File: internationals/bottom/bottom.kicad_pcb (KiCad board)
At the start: 2 copper layers, 1 part, among them U1 ESP-S2-Pico

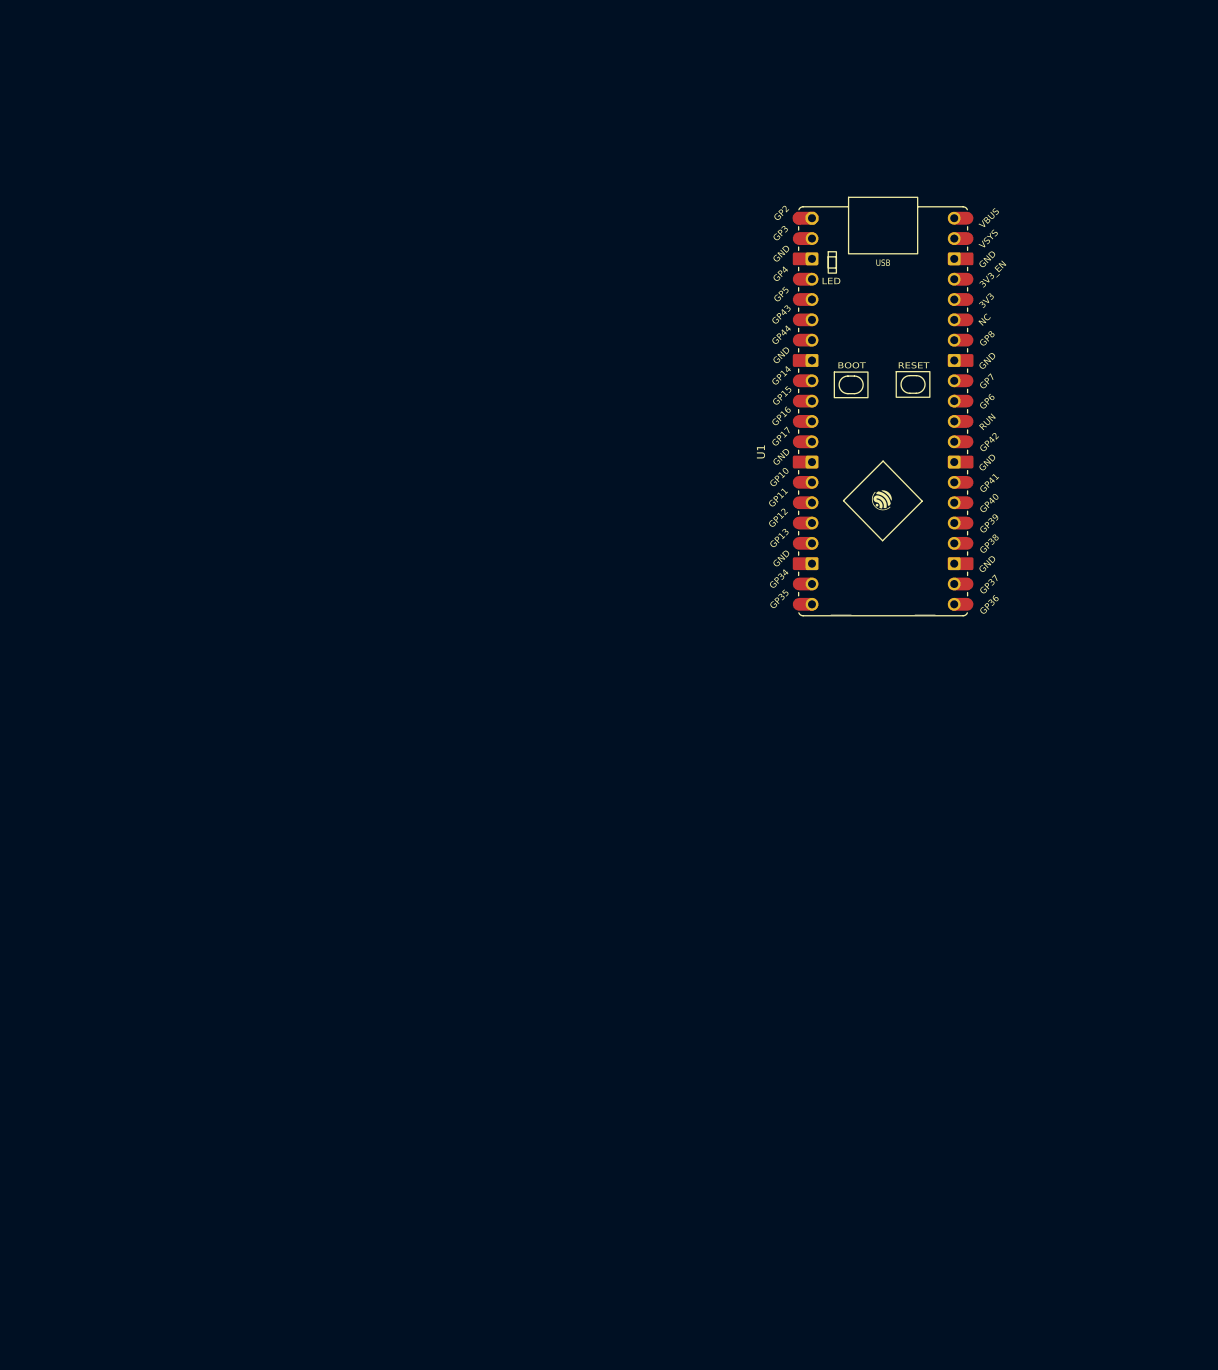
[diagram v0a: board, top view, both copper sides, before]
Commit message: pcbs: bottom: feat: add pcb with parts placed, left with routing
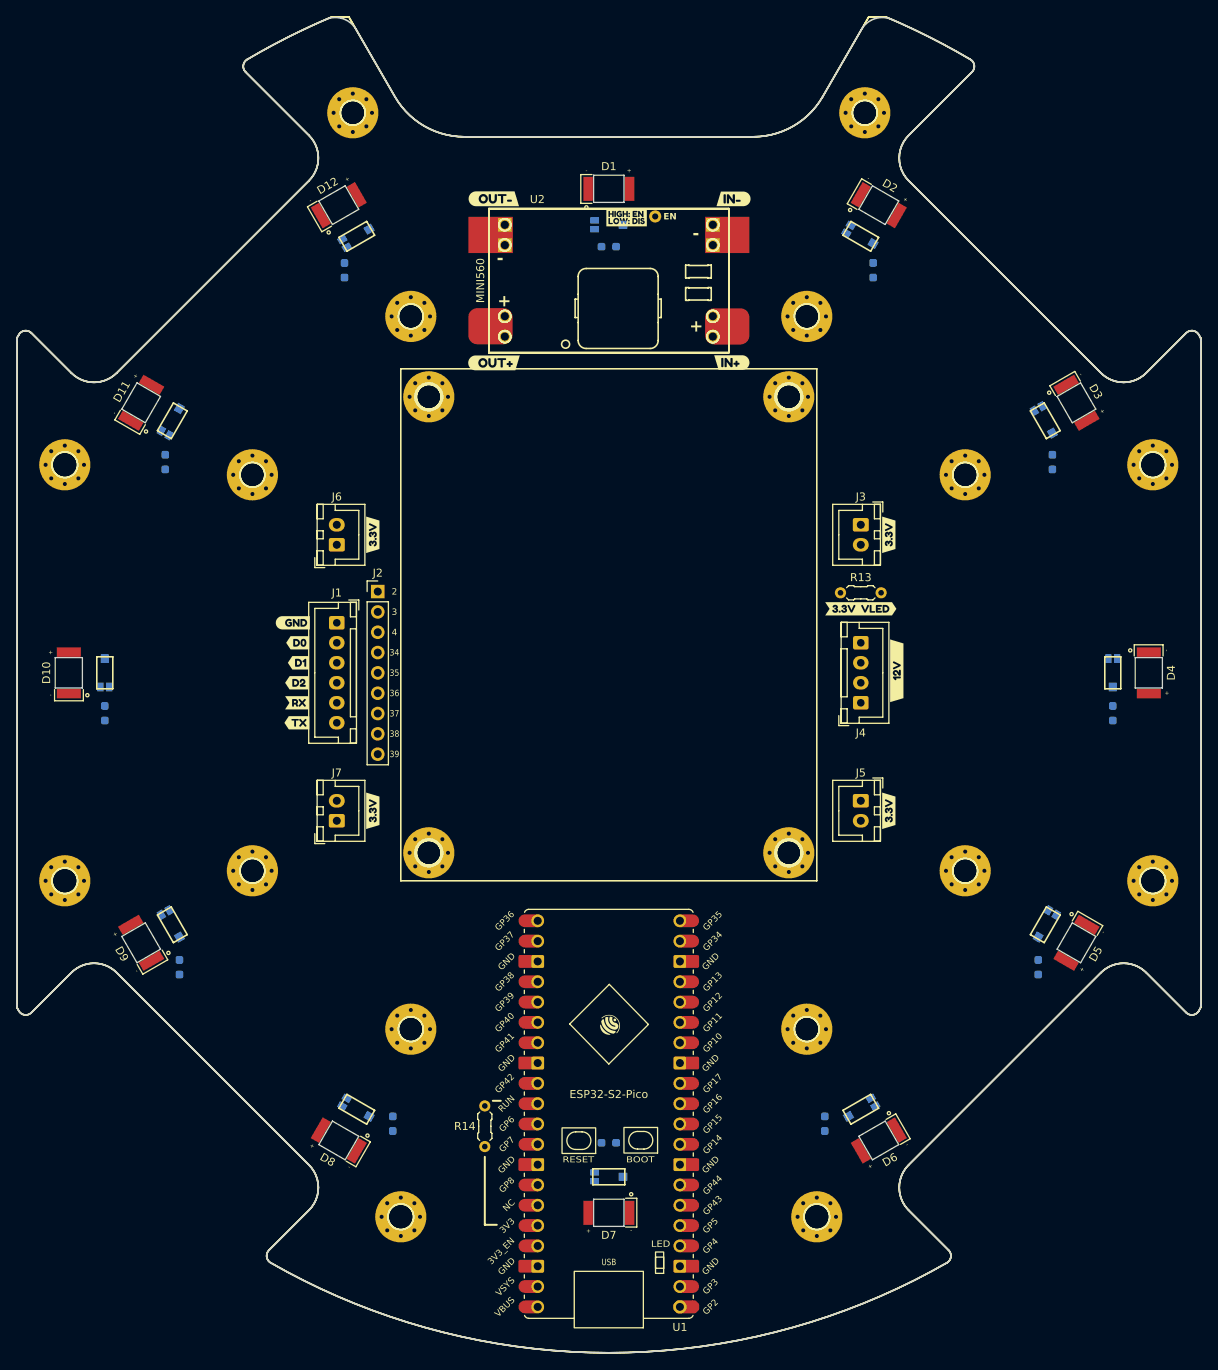
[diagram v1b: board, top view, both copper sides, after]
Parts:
- added D1: LED, PorridgePi-Personal:LED-6028-SMD, F.Cu at (100.0, 39.5)
- added D10: LED, PorridgePi-Personal:LED-6028-SMD, F.Cu at (32.5, 100.0)
- added D11: LED, PorridgePi-Personal:LED-6028-SMD, F.Cu at (41.5, 66.2)
- added D12: LED, PorridgePi-Personal:LED-6028-SMD, F.Cu at (66.2, 41.5)
- added D2: LED, PorridgePi-Personal:LED-6028-SMD, F.Cu at (133.8, 41.5)
- added D3: LED, PorridgePi-Personal:LED-6028-SMD, F.Cu at (158.5, 66.2)
- added D4: LED, PorridgePi-Personal:LED-6028-SMD, F.Cu at (167.5, 100.0)
- added D5: LED, PorridgePi-Personal:LED-6028-SMD, F.Cu at (158.5, 133.8)
- added D6: LED, PorridgePi-Personal:LED-6028-SMD, F.Cu at (133.8, 158.5)
- added D7: LED, PorridgePi-Personal:LED-6028-SMD, F.Cu at (100.0, 167.5)
- added D8: LED, PorridgePi-Personal:LED-6028-SMD, F.Cu at (66.2, 158.5)
- added D9: LED, PorridgePi-Personal:LED-6028-SMD, F.Cu at (41.5, 133.8)
- added H1: MountingHole-M3, MountingHole:MountingHole_3.2mm_M3_Pad_Via, F.Cu at (68.0, 30.0)
- added H10: MountingHole-M3, MountingHole:MountingHole_3.2mm_M3_Pad_Via, F.Cu at (55.5, 75.3)
- added H11: MountingHole-M3, MountingHole:MountingHole_3.2mm_M3_Pad_Via, F.Cu at (55.5, 124.7)
- added H12: MountingHole-M3, MountingHole:MountingHole_3.2mm_M3_Pad_Via, F.Cu at (75.3, 144.5)
- added H13: MountingHole-M3, MountingHole:MountingHole_3.2mm_M3_Pad_Via, F.Cu at (144.5, 75.3)
- added H14: MountingHole-M3, MountingHole:MountingHole_3.2mm_M3_Pad_Via, F.Cu at (144.5, 124.7)
- added H15: MountingHole-M3, MountingHole:MountingHole_3.2mm_M3_Pad_Via, F.Cu at (124.7, 144.5)
- added H16: MountingHole-M3, MountingHole:MountingHole_3.2mm_M3_Pad_Via, F.Cu at (124.7, 55.5)
- added H17: MountingHole-M3, MountingHole:MountingHole_3.2mm_M3_Pad_Via, F.Cu at (122.5, 122.5)
- added H18: MountingHole-M3, MountingHole:MountingHole_3.2mm_M3_Pad_Via, F.Cu at (77.5, 122.5)
- added H19: MountingHole-M3, MountingHole:MountingHole_3.2mm_M3_Pad_Via, F.Cu at (77.5, 65.5)
- added H2: MountingHole-M3, MountingHole:MountingHole_3.2mm_M3_Pad_Via, F.Cu at (132.0, 30.0)
- added H20: MountingHole-M3, MountingHole:MountingHole_3.2mm_M3_Pad_Via, F.Cu at (122.5, 65.5)
- added H3: MountingHole-M3, MountingHole:MountingHole_3.2mm_M3_Pad_Via, F.Cu at (168.0, 74.0)
- added H4: MountingHole-M3, MountingHole:MountingHole_3.2mm_M3_Pad_Via, F.Cu at (168.0, 126.0)
- added H5: MountingHole-M3, MountingHole:MountingHole_3.2mm_M3_Pad_Via, F.Cu at (126.0, 168.0)
- added H6: MountingHole-M3, MountingHole:MountingHole_3.2mm_M3_Pad_Via, F.Cu at (74.0, 168.0)
- added H7: MountingHole-M3, MountingHole:MountingHole_3.2mm_M3_Pad_Via, F.Cu at (32.0, 74.0)
- added H8: MountingHole-M3, MountingHole:MountingHole_3.2mm_M3_Pad_Via, F.Cu at (32.0, 126.0)
- added H9: MountingHole-M3, MountingHole:MountingHole_3.2mm_M3_Pad_Via, F.Cu at (75.3, 55.5)
- added J1: JST-XH-B6B, Connector_JST:JST_XH_B6B-XH-A_1x06_P2.50mm_Vertical, F.Cu at (66.0, 93.8)
- added J2: Header-01x09, Connector_PinHeader_2.54mm:PinHeader_1x09_P2.54mm_Vertical, F.Cu at (71.1, 89.8)
- added J3: 3.3V-JST-XH-B2B, Connector_JST:JST_XH_B2B-XH-A_1x02_P2.50mm_Vertical, F.Cu at (131.5, 81.5)
- added J4: JST-XH-B4B, Connector_JST:JST_XH_B4B-XH-A_1x04_P2.50mm_Vertical, F.Cu at (131.5, 103.8)
- added J5: 3.3V-JST-XH-B2B, Connector_JST:JST_XH_B2B-XH-A_1x02_P2.50mm_Vertical, F.Cu at (131.5, 116.0)
- added J6: 3.3V-JST-XH-B2B, Connector_JST:JST_XH_B2B-XH-A_1x02_P2.50mm_Vertical, F.Cu at (66.0, 84.0)
- added J7: 3.3V-JST-XH-B2B, Connector_JST:JST_XH_B2B-XH-A_1x02_P2.50mm_Vertical, F.Cu at (66.0, 118.5)
- added L1: TEMT6000, PorridgePi-Personal:TEMT6000-SMD, B.Cu at (100.0, 44.0)
- added L10: TEMT6000, PorridgePi-Personal:TEMT6000-SMD, B.Cu at (37.0, 100.0)
- added L11: TEMT6000, PorridgePi-Personal:TEMT6000-SMD, B.Cu at (45.4, 68.5)
- added L12: TEMT6000, PorridgePi-Personal:TEMT6000-SMD, B.Cu at (68.5, 45.4)
- added L2: TEMT6000, PorridgePi-Personal:TEMT6000-SMD, B.Cu at (131.5, 45.4)
- added L3: TEMT6000, PorridgePi-Personal:TEMT6000-SMD, B.Cu at (154.6, 68.5)
- added L4: TEMT6000, PorridgePi-Personal:TEMT6000-SMD, B.Cu at (163.0, 100.0)
- added L5: TEMT6000, PorridgePi-Personal:TEMT6000-SMD, B.Cu at (154.6, 131.5)
- added L6: TEMT6000, PorridgePi-Personal:TEMT6000-SMD, B.Cu at (131.5, 154.6)
- added L7: TEMT6000, PorridgePi-Personal:TEMT6000-SMD, B.Cu at (100.0, 163.0)
- added L8: TEMT6000, PorridgePi-Personal:TEMT6000-SMD, B.Cu at (68.5, 154.6)
- added L9: TEMT6000, PorridgePi-Personal:TEMT6000-SMD, B.Cu at (45.4, 131.5)
- added R1: 10k, Resistor_SMD:R_0603_1608Metric_Pad0.98x0.95mm_HandSolder, B.Cu at (100.0, 46.7)
- added R10: 10k, Resistor_SMD:R_0603_1608Metric_Pad0.98x0.95mm_HandSolder, B.Cu at (37.0, 105.1)
- added R11: 10k, Resistor_SMD:R_0603_1608Metric_Pad0.98x0.95mm_HandSolder, B.Cu at (44.6, 73.7)
- added R12: 10k, Resistor_SMD:R_0603_1608Metric_Pad0.98x0.95mm_HandSolder, B.Cu at (67.0, 49.7)
- added R13: R, PCM_Resistor_THT_AKL:R_Axial_DIN0204_L3.6mm_D1.6mm_P5.08mm_Horizontal, F.Cu at (129.0, 90.0)
- added R14: R, PCM_Resistor_THT_AKL:R_Axial_DIN0204_L3.6mm_D1.6mm_P5.08mm_Horizontal, F.Cu at (84.5, 154.1)
- added R2: 10k, Resistor_SMD:R_0603_1608Metric_Pad0.98x0.95mm_HandSolder, B.Cu at (133.0, 49.7)
- added R3: 10k, Resistor_SMD:R_0603_1608Metric_Pad0.98x0.95mm_HandSolder, B.Cu at (155.4, 73.7)
- added R4: 10k, Resistor_SMD:R_0603_1608Metric_Pad0.98x0.95mm_HandSolder, B.Cu at (163.0, 105.1)
- added R5: 10k, Resistor_SMD:R_0603_1608Metric_Pad0.98x0.95mm_HandSolder, B.Cu at (153.7, 136.8)
- added R6: 10k, Resistor_SMD:R_0603_1608Metric_Pad0.98x0.95mm_HandSolder, B.Cu at (127.0, 156.4)
- added R7: 10k, Resistor_SMD:R_0603_1608Metric_Pad0.98x0.95mm_HandSolder, B.Cu at (100.0, 158.8)
- added R8: 10k, Resistor_SMD:R_0603_1608Metric_Pad0.98x0.95mm_HandSolder, B.Cu at (73.0, 156.4)
- added R9: 10k, Resistor_SMD:R_0603_1608Metric_Pad0.98x0.95mm_HandSolder, B.Cu at (46.3, 136.8)
- added U2: MINI560 3.3V, PorridgePi-Personal:MINI560, F.Cu at (87.0, 44.0)
- added kibuzzard-6669C5DE: G***, kibuzzard-6669C5DE, F.Cu at (131.5, 92.0)
- added kibuzzard-6669C5ED: G***, kibuzzard-6669C5ED, F.Cu at (70.5, 82.8)
- added kibuzzard-6669C5ED: G***, kibuzzard-6669C5ED, F.Cu at (135.0, 82.8)
- added kibuzzard-6669C5ED: G***, kibuzzard-6669C5ED, F.Cu at (135.0, 117.2)
- added kibuzzard-6669C5ED: G***, kibuzzard-6669C5ED, F.Cu at (70.5, 117.2)
- added kibuzzard-6669C688: G***, kibuzzard-6669C688, F.Cu at (136.0, 99.8)
- added kibuzzard-6669C6B5: G***, kibuzzard-6669C6B5, F.Cu at (61.2, 98.8)
- added kibuzzard-6669C6DE: G***, kibuzzard-6669C6DE, F.Cu at (61.0, 103.8)
- added kibuzzard-6669C6E8: G***, kibuzzard-6669C6E8, F.Cu at (61.0, 106.2)
- added kibuzzard-6669C6EF: G***, kibuzzard-6669C6EF, F.Cu at (60.5, 93.8)
- added kibuzzard-6669C702: G***, kibuzzard-6669C702, F.Cu at (61.1, 96.2)
- added kibuzzard-6669C706: G***, kibuzzard-6669C706, F.Cu at (61.0, 101.2)
- added kibuzzard-6669C956: G***, kibuzzard-6669C956, B.Cu at (129.2, 117.2)
- added kibuzzard-6669C956: G***, kibuzzard-6669C956, B.Cu at (63.5, 82.8)
- added kibuzzard-6669C956: G***, kibuzzard-6669C956, B.Cu at (63.5, 117.2)
- added kibuzzard-6669C956: G***, kibuzzard-6669C956, B.Cu at (129.2, 82.8)
- added kibuzzard-6669C9E8: G***, kibuzzard-6669C9E8, B.Cu at (128.5, 100.0)
- moved U1 137.1 mm to (108.9, 179.3), turned to 180 degrees
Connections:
- U1 pad 1: unconnected-(U1-GPIO2-ADC1_1-Pad1) -> GPIO2
- U1 pad 10: unconnected-(U1-GPIO15-ADC2_4-Pad10) -> TEMT3
- U1 pad 11: unconnected-(U1-GPIO16-ADC2_5-Pad11) -> TEMT4
- U1 pad 12: unconnected-(U1-GPIO17-ADC2_6-Pad12) -> TEMT5
- U1 pad 13: unconnected-(U1-GND-Pad13) -> GND
- U1 pad 14: unconnected-(U1-GPIO10-ADC1_9-Pad14) -> TEMT6
- U1 pad 15: unconnected-(U1-GPIO11-ADC2_0-Pad15) -> TEMT7
- U1 pad 16: unconnected-(U1-GPIO12-ADC2_1-Pad16) -> TEMT8
- U1 pad 17: unconnected-(U1-GPIO13-ADC2_2-Pad17) -> TEMT9
- U1 pad 18: unconnected-(U1-GND-Pad18) -> GND
- U1 pad 19: unconnected-(U1-GPIO34-Pad19) -> GPIO34
- U1 pad 2: unconnected-(U1-GPIO3-ADC1_2-Pad2) -> GPIO3
- U1 pad 20: unconnected-(U1-GPIO35-Pad20) -> GPIO35
- U1 pad 21: unconnected-(U1-GPIO36-Pad21) -> GPIO36
- U1 pad 22: unconnected-(U1-GPIO37-Pad22) -> GPIO37
- U1 pad 23: unconnected-(U1-GND-Pad23) -> GND
- U1 pad 24: unconnected-(U1-GPIO38-Pad24) -> GPIO38
- U1 pad 25: unconnected-(U1-GPIO39-Pad25) -> GPIO39
- U1 pad 26: unconnected-(U1-GPIO40-Pad26) -> Bottom-D2
- U1 pad 27: unconnected-(U1-GPIO41-Pad27) -> Bottom-D1
- U1 pad 28: unconnected-(U1-GND-Pad28) -> GND
- U1 pad 29: unconnected-(U1-GPIO42-Pad29) -> Bottom-D0
- U1 pad 3: unconnected-(U1-GND-Pad3) -> GND
- U1 pad 30: unconnected-(U1-RUN-Pad30) -> Net-(U1-RUN)
- U1 pad 31: unconnected-(U1-GPIO6-ADC1_5-Pad31) -> TEMT10
- U1 pad 32: unconnected-(U1-GPIO7-ADC1_6-Pad32) -> TEMT11
- U1 pad 33: unconnected-(U1-GND-Pad33) -> GND
- U1 pad 34: unconnected-(U1-GPIO8-ADC1_7-Pad34) -> TEMT12
- U1 pad 36: unconnected-(U1-3V3-Pad36) -> Net-(U1-3V3)
- U1 pad 38: unconnected-(U1-GND-Pad38) -> GND
- U1 pad 39: unconnected-(U1-VSYS-Pad39) -> +3.3V
- U1 pad 4: unconnected-(U1-GPIO4-ADC1_3-Pad4) -> GPIO4
- U1 pad 5: unconnected-(U1-GPIO5-ADC1_4-Pad5) -> TEMT1
- U1 pad 6: unconnected-(U1-GPIO43-Pad6) -> Bottom-TX0-Top-RX
- U1 pad 7: unconnected-(U1-GPIO44-Pad7) -> Bottom-RX0-Top-TX
- U1 pad 8: unconnected-(U1-GND-Pad8) -> GND
- U1 pad 9: unconnected-(U1-GPIO14-ADC2_3-Pad9) -> TEMT2
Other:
- board outline added: 148 x 166.9 mm
- board text added: "2"
- board text added: "3"
- board text added: "3.3V"
- board text added: "34"
- board text added: "35"
- board text added: "36"
- board text added: "37"
- board text added: "38"
- board text added: "39"
- board text added: "4"
- board text added: "D0"
- board text added: "D1"
- board text added: "D2"
- board text added: "GND"
- board text added: "RX"
- board text added: "TX"
- board text added: "VLED"
